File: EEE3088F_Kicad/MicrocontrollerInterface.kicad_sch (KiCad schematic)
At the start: 16 parts, among them J1 USB_B_Micro, U1 CAT24C256, U2 INTERFACE-CP2102-GMR(QFN28), U3 STM32F051C6Tx

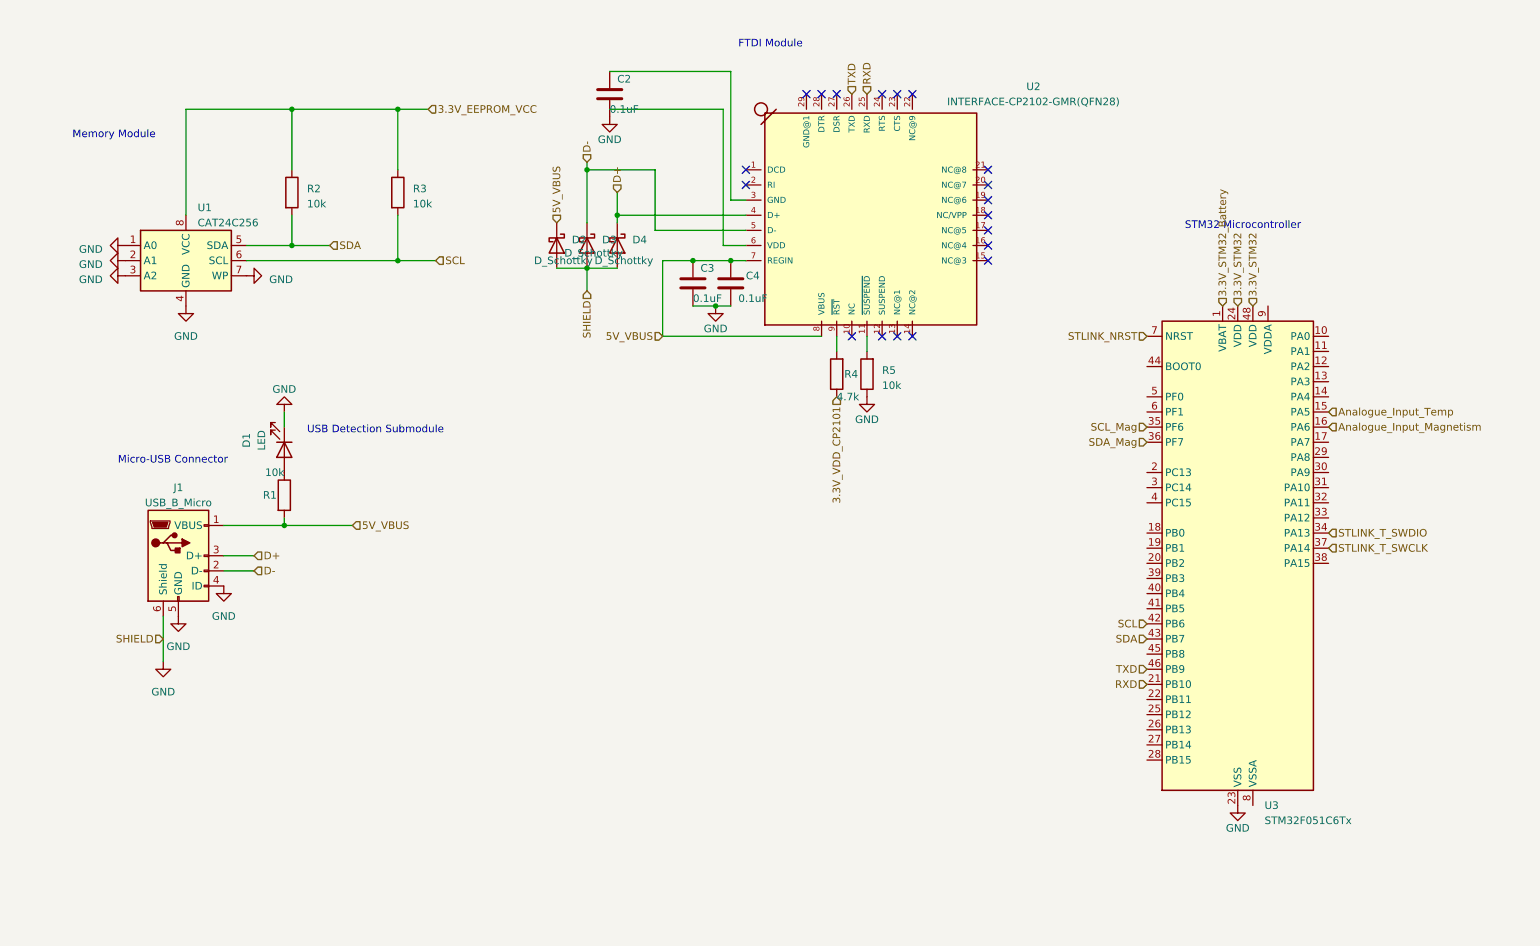
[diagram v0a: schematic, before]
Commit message: I have updated the microncontroller interface
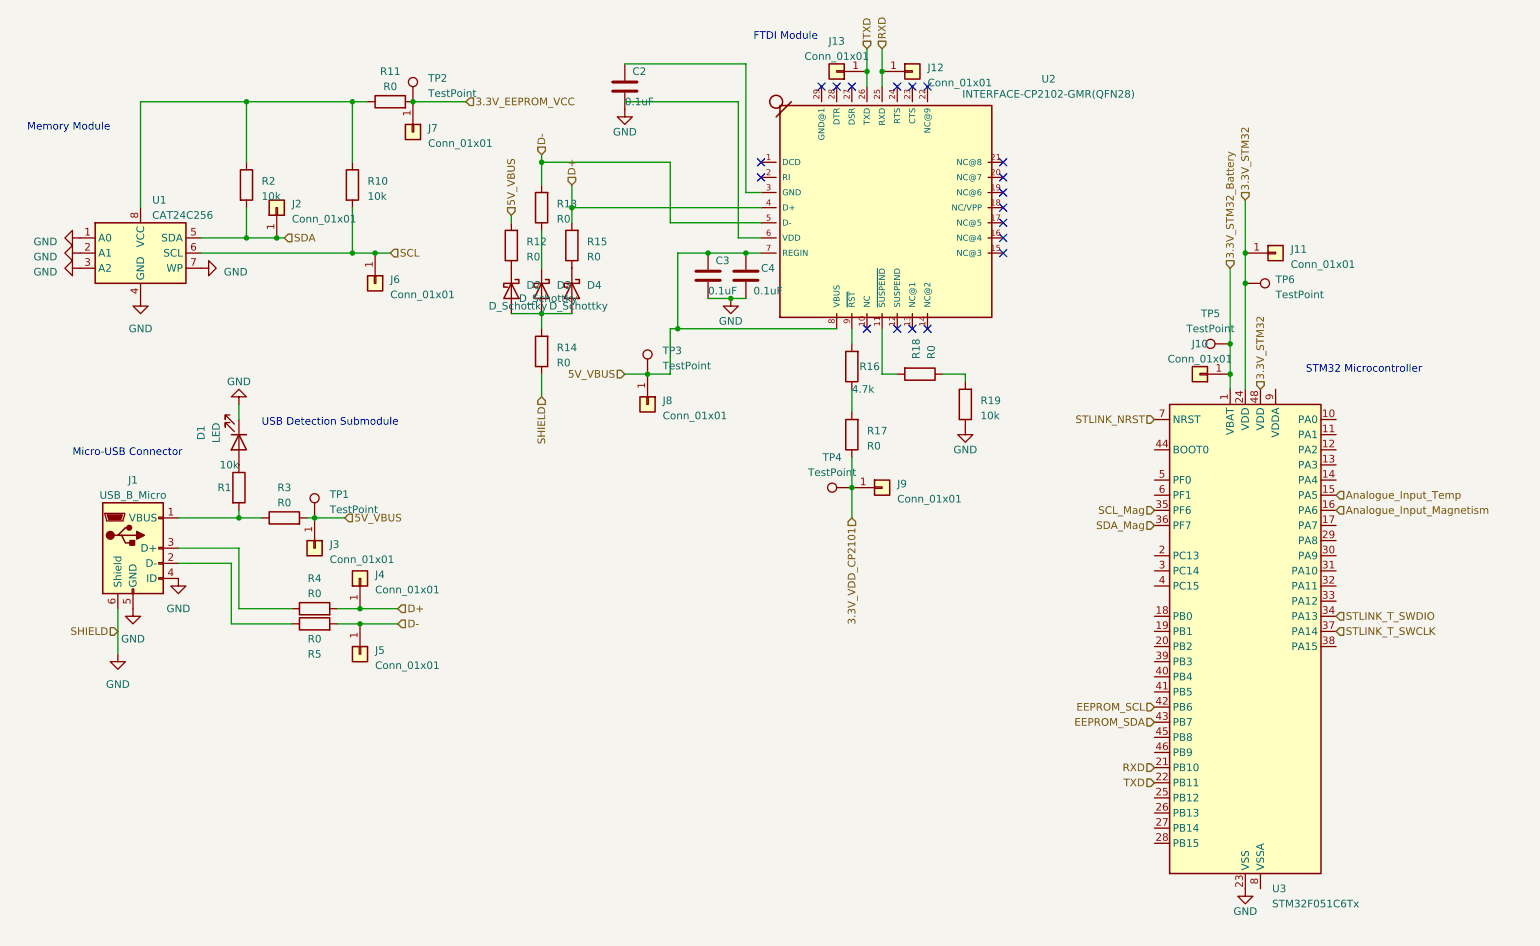
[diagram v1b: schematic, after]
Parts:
- added J10, J11, J12, J13, J2, J3, J4, J5, J6, J7, J8, J9: Conn_01x01, symbol Connector_Generic:Conn_01x01
- added R10, R19: 10k, symbol Device:R
- added R11, R12, R13, R14, R15, R17, R18: R0, symbol Device:R
- added R16: 4.7k, symbol Device:R
- added TP1, TP2, TP3, TP4, TP5, TP6: TestPoint, symbol Connector:TestPoint
- R3, R5: value 10k -> R0
- R4: value 4.7k -> R0
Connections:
- net 3.3V_EEPROM_VCC: now also J7.1 (Pin_1), R11.2, TP2.1; no longer R2.1, R3.1, U1.8 (VCC)
- net 3.3V_STM32: now also J11.1 (Pin_1), TP6.1
- net 3.3V_STM32_Battery: now also J10.1 (Pin_1), TP5.1
- net 3.3V_VDD_CP2101: now also J9.1 (Pin_1), R17.1, TP4.1; no longer R4.1
- net 5V_VBUS: now also R3.2, J3.1 (Pin_1), J8.1 (Pin_1), R12.2, TP1.1, TP3.1; no longer D2.1 (K), J1.1 (VBUS), R1.2
- net D+: now also R4.2, J4.1 (Pin_1), R15.2; no longer D4.1 (K), J1.3 (D+)
- net D-: now also R5.2, J5.1 (Pin_1), R13.2; no longer D3.1 (K), J1.2 (D-)
- net GND: now also R14.1, R19.1; no longer D2.2 (A), D3.2 (A), D4.2 (A), R5.1
- net RXD: now also J12.1 (Pin_1)
- net SCL: now also J6.1 (Pin_1), R10.2; no longer R3.2, U3.42 (PB6)
- net SDA: now also J2.1 (Pin_1); no longer U3.43 (PB7)
- net TXD: now also U3.22 (PB11), J13.1 (Pin_1); no longer U3.46 (PB9)
- net at U2.9 (~{RST}): now also R16.2; no longer R4.2
- net at U2.11 (~{SUSPEND}): now also R18.2; no longer R5.2
- new net: D3.1 (K), R13.1
- new net: R16.1, R17.2
- new net: D2.2 (A), D3.2 (A), D4.2 (A), R14.2
- new net: D4.1 (K), R15.1
- new net: R10.1, R11.1, R2.1, U1.8 (VCC)
- new net: J1.1 (VBUS), R1.2, R3.1
- new net: J1.2 (D-), R5.1
- new net: J1.3 (D+), R4.1
- new net: R18.1, R19.2
- new net: D2.1 (K), R12.1
- new net EEPROM_SCL: U3.42 (PB6)
- new net EEPROM_SDA: U3.43 (PB7)

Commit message: Microntroller Update
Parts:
- removed C2, C3, C4: 0.1uF, symbol Device:C
- removed D1: LED, symbol Device:LED
- removed D2, D3, D4: D_Schottky, symbol Device:D_Schottky
- removed J1: USB_B_Micro, symbol Connector:USB_B_Micro
- removed J10, J11, J12, J13, J2, J3, J4, J5, J6, J7, J8, J9: Conn_01x01, symbol Connector_Generic:Conn_01x01
- removed R1, R10, R2: 10k, symbol Device:R
- removed R11, R3, R4, R5: R0, symbol Device:R
- removed TP1, TP2, TP3, TP4, TP5, TP6: TestPoint, symbol Connector:TestPoint
- added C5, C6, C7: 0.1uF, symbol Device:C
- added D4: LED, symbol Device:LED
- added D5, D6, D7: D_Schottky, symbol Device:D_Schottky
- added J6: USB_B_Micro, MICROXNJ:SHOUHAN_MICROXNJ, symbol Connector:USB_B_Micro
- added R20, R21, R22, R24, R25, R27, R28: R0, symbol Device:R
- added R23: 4.7k, symbol Device:R
- added R26: 10k, symbol Device:R
- added TP10, TP11, TP12, TP13, TP14, TP15, TP16, TP7, TP8, TP9: TestPoint, symbol Connector:TestPoint
- R12, R13, R17: value R0 -> 10k; LCSC (none) -> C17902
- R14, R15, R18: LCSC (none) -> C17888
- R16: value 4.7k -> R0; LCSC (none) -> C17888
- R19: value 10k -> R0; LCSC (none) -> C17888
- U1: footprint (none) -> EEPROM:SOIC127P600X175-8N; LCSC (none) -> C6482
- U2: footprint QFN28G_0.5-5X5MM -> USB UART Chip:QFN28G_0.5-5X5MM; LCSC (none) -> C6568
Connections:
- net 3.3V_EEPROM_VCC: now also R18.2, TP10.1
- net 3.3V_STM32: now also R28.2; no longer U3.24 (VDD)
- net 3.3V_STM32_Battery: now also R27.2; no longer U3.1 (VBAT)
- net 3.3V_VDD_CP2101: now also R24.1, TP12.1; no longer R17.1
- net 5V_VBUS: now also R14.2, R19.2, C6.1, C7.1, TP11.1, TP7.1; no longer R12.2
- net D+: now also R22.2, TP8.1
- net D-: now also R16.2, R20.2, TP9.1; no longer R13.2
- net GND: now also C5.2, C6.2, C7.2, D4.1 (K), J6.4 (ID), J6.5 (GND), J6.6 (Shield), R21.1, R26.1; no longer R14.1, R19.1
- net RXD: now also TP14.1
- net SCL: now also R17.2
- net SDA: now also R13.2
- net TXD: now also TP13.1
- net at R13.1: now also R17.1, R18.1, U1.8 (VCC)
- net at R16.1: now also J6.2 (D-); no longer R17.2
- net at U2.9 (~{RST}): now also R23.2; no longer R16.2
- net at R15.1: now also J6.3 (D+)
- net at U2.3 (GND): now also C5.1
- net at R12.1: now also D4.2 (A)
- net at U2.11 (~{SUSPEND}): now also R25.2; no longer R18.2
- new net: R27.1, TP15.1, U3.1 (VBAT)
- new net: D5.2 (A), D6.2 (A), D7.2 (A), R21.2
- new net: D5.1 (K), R19.1
- new net: R25.1, R26.2
- new net: J6.1 (VBUS), R12.2, R14.1
- new net: D7.1 (K), R22.1
- new net: R28.1, TP16.1, U3.24 (VDD)
- new net: D6.1 (K), R20.1
- new net: R23.1, R24.2

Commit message: I have updated microcontoller and comments
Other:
- note added: "EEPROM chip that allows the environmental data to be stored to be retrived at a later date"
- note added: "STM32 micronctroller that facillites all the features of the device such as the retrieval of environmental as it communicates with the sensors and stores the data"
- note added: "The micro-USB Connector connects the board and STM32 microcontroller to the computer to facilate power and data transfer"
- note added: "This chip connects to the USB connector and allows the USB to interface with the STM32 microcontroller"
- title: (none) -> Microcontroller Interface
- moved on the sheet: D5, D6, R19, R20
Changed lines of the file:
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@@
 (kicad_sch (version 20230121) (generator eeschema)
   (paper "A4")
+  (title_block
+    (title "Microcontroller Interface")
+  )
   (junction (at 144.78 54.61) (diameter 0) (color 0 0 0 0)
   )
@@
   (junction (at 226.06 69.85) (diameter 0) (color 0 0 0 0)
   )
-  (junction (at 110.49 64.77) (diameter 0) (color 0 0 0 0)
+  (junction (at 106.68 64.77) (diameter 0) (color 0 0 0 0)
   )
   (junction (at 167.64 22.86) (diameter 0) (color 0 0 0 0)
@@
   (junction (at 81.28 114.3) (diameter 0) (color 0 0 0 0)
   )
-  (junction (at 110.49 39.37) (diameter 0) (color 0 0 0 0)
+  (junction (at 106.68 39.37) (diameter 0) (color 0 0 0 0)
   )
   (junction (at 228.6 59.69) (diameter 0) (color 0 0 0 0)
@@
   (no_connect (at 170.18 26.67))
   (no_connect (at 187.96 39.37))
-  (wire (pts (xy 110.49 39.37) (xy 110.49 43.18))
+  (wire (pts (xy 106.68 39.37) (xy 106.68 43.18))
     (stroke (width 0) (type default))
   )
@@
     (stroke (width 0) (type default))
   )
-  (wire (pts (xy 110.49 50.8) (xy 110.49 57.15))
+  (wire (pts (xy 106.68 50.8) (xy 106.68 57.15))
     (stroke (width 0) (type default))
   )
@@
     (stroke (width 0) (type default))
   )
-  (wire (pts (xy 110.49 38.1) (xy 110.49 39.37))
+  (wire (pts (xy 106.68 38.1) (xy 106.68 39.37))
     (stroke (width 0) (type default))
   )
@@
     (stroke (width 0) (type default))
   )
-  (wire (pts (xy 110.49 64.77) (xy 115.57 64.77))
+  (wire (pts (xy 106.68 64.77) (xy 115.57 64.77))
     (stroke (width 0) (type default))
   )
@@
     (stroke (width 0) (type default))
   )
+  (wire (pts (xy 106.68 66.04) (xy 110.49 66.04))
+    (stroke (width 0) (type default))
+  )
   (wire (pts (xy 167.64 19.05) (xy 167.64 22.86))
     (stroke (width 0) (type default))
@@
     (stroke (width 0) (type default))
   )
-  (wire (pts (xy 105.41 49.53) (xy 105.41 48.26))
+  (wire (pts (xy 95.25 49.53) (xy 95.25 48.26))
     (stroke (width 0) (type default))
   )
@@
     (stroke (width 0) (type default))
   )
-  (wire (pts (xy 110.49 64.77) (xy 110.49 67.31))
+  (wire (pts (xy 106.68 64.77) (xy 106.68 66.04))
     (stroke (width 0) (type default))
   )
@@
     (stroke (width 0) (type default))
   )
-  (wire (pts (xy 132.08 39.37) (xy 110.49 39.37))
+  (wire (pts (xy 132.08 39.37) (xy 106.68 39.37))
     (stroke (width 0) (type default))
   )
@@
     (stroke (width 0) (type default))
   )
-  (wire (pts (xy 105.41 64.77) (xy 110.49 64.77))
+  (wire (pts (xy 95.25 64.77) (xy 106.68 64.77))
     (stroke (width 0) (type default))
   )
@@
     (stroke (width 0) (type default))
   )
+  (wire (pts (xy 110.49 66.04) (xy 110.49 67.31))
+    (stroke (width 0) (type default))
+  )
   (wire (pts (xy 162.56 81.28) (xy 162.56 77.47))
     (stroke (width 0) (type default))
@@
   (wire (pts (xy 165.1 19.05) (xy 165.1 22.86))
     (stroke (width 0) (type default))
+  )
+  (text "STM32 micronctroller that facillites all the features\nof the device such as the retrieval of environmental\nas it communicates with the sensors and stores the data"
+    (at 153.67 148.59 0)
+    (effects (font (size 1.27 1.27)) (justify left bottom))
   )
   (text "STM32 Microcontroller" (at 238.76 74.93 0)
@@
     (effects (font (size 1.27 1.27)) (justify left bottom))
   )
+  (text "The micro-USB Connector connects the board and STM32 microcontroller\nto the computer to facilate power and data transfer"
+    (at 31.75 135.89 0)
+    (effects (font (size 1.27 1.27)) (justify left bottom))
+  )
   (text "USB Detection Submodule" (at 63.5 83.82 0)
     (effects (font (size 1.27 1.27)) (justify left bottom))
   )
+  (text "EEPROM chip that allows the environmental data\nto be stored to be retrived at a later date"
+    (at 26.67 72.39 0)
+    (effects (font (size 1.27 1.27)) (justify left bottom))
+  )
+  (text "This chip connects to the USB connector and allows the \nUSB to interface with the STM32 microcontroller"
+    (at 102.87 92.71 0)
+    (effects (font (size 1.27 1.27)) (justify left bottom))
+  )
   (text "FTDI Module" (at 146.05 19.05 0)
     (effects (font (size 1.27 1.27)) (justify left bottom))
@@
     (effects (font (size 1.27 1.27)) (justify left))
   )
-  (hierarchical_label "5V_VBUS" (shape input) (at 105.41 48.26 90) (fields_autoplaced)
+  (hierarchical_label "5V_VBUS" (shape input) (at 95.25 48.26 90) (fields_autoplaced)
     (effects (font (size 1.27 1.27)) (justify left))
   )
@@
     (effects (font (size 1.27 1.27)) (justify left))
   )
-  (hierarchical_label "D-" (shape input) (at 110.49 38.1 90) (fields_autoplaced)
+  (hierarchical_label "D-" (shape input) (at 106.68 38.1 90) (fields_autoplaced)
     (effects (font (size 1.27 1.27)) (justify left))
   )
@@
     )
   )
-  (symbol (lib_id "Device:D_Schottky") (at 105.41 60.96 270) (unit 1)
+  (symbol (lib_id "Device:D_Schottky") (at 95.25 60.96 270) (unit 1)
     (in_bom yes) (on_board yes) (dnp no)
-    (property "Reference" "D5" (at 107.95 60.0075 90)
-      (effects (font (size 1.27 1.27)) (justify left))
-    )
-    (property "Value" "D_Schottky" (at 101.6 63.5 90)
-      (effects (font (size 1.27 1.27)) (justify left))
-    )
-    (property "Footprint" "" (at 105.41 60.96 0)
-      (effects (font (size 1.27 1.27)) hide)
-    )
-    (property "Datasheet" "~" (at 105.41 60.96 0)
-      (effects (font (size 1.27 1.27)) hide)
-    )
-    (property "LCSC" "C7074" (at 105.41 60.96 0)
+    (property "Reference" "D5" (at 97.79 60.0075 90)
+      (effects (font (size 1.27 1.27)) (justify left))
+    )
+    (property "Value" "D_Schottky" (at 91.44 63.5 90)
+      (effects (font (size 1.27 1.27)) (justify left))
+    )
+    (property "Footprint" "" (at 95.25 60.96 0)
+      (effects (font (size 1.27 1.27)) hide)
+    )
+    (property "Datasheet" "~" (at 95.25 60.96 0)
+      (effects (font (size 1.27 1.27)) hide)
+    )
+    (property "LCSC" "C7074" (at 95.25 60.96 0)
       (effects (font (size 1.27 1.27)) hide)
     )
@@
     )
   )
-  (symbol (lib_id "Device:D_Schottky") (at 110.49 60.96 270) (unit 1)
+  (symbol (lib_id "Device:D_Schottky") (at 106.68 60.96 270) (unit 1)
     (in_bom yes) (on_board yes) (dnp no)
-    (property "Reference" "D6" (at 113.03 60.0075 90)
-      (effects (font (size 1.27 1.27)) (justify left))
-    )
-    (property "Value" "D_Schottky" (at 106.68 62.23 90)
-      (effects (font (size 1.27 1.27)) (justify left))
-    )
-    (property "Footprint" "" (at 110.49 60.96 0)
-      (effects (font (size 1.27 1.27)) hide)
-    )
-    (property "Datasheet" "~" (at 110.49 60.96 0)
-      (effects (font (size 1.27 1.27)) hide)
-    )
-    (property "LCSC" "C7074" (at 110.49 60.96 0)
+    (property "Reference" "D6" (at 109.22 60.0075 90)
+      (effects (font (size 1.27 1.27)) (justify left))
+    )
+    (property "Value" "D_Schottky" (at 102.87 55.88 90)
+      (effects (font (size 1.27 1.27)) (justify left))
+    )
+    (property "Footprint" "" (at 106.68 60.96 0)
+      (effects (font (size 1.27 1.27)) hide)
+    )
+    (property "Datasheet" "~" (at 106.68 60.96 0)
+      (effects (font (size 1.27 1.27)) hide)
+    )
+    (property "LCSC" "C7074" (at 106.68 60.96 0)
       (effects (font (size 1.27 1.27)) hide)
     )
@@
     )
   )
-  (symbol (lib_id "Device:R") (at 105.41 53.34 180) (unit 1)
-    (in_bom yes) (on_board yes) (dnp no) (fields_autoplaced)
-    (property "Reference" "R19" (at 107.95 52.705 0)
-      (effects (font (size 1.27 1.27)) (justify right))
-    )
-    (property "Value" "R0" (at 107.95 55.245 0)
-      (effects (font (size 1.27 1.27)) (justify right))
-    )
-    (property "Footprint" "" (at 107.188 53.34 90)
-      (effects (font (size 1.27 1.27)) hide)
-    )
-    (property "Datasheet" "~" (at 105.41 53.34 0)
-      (effects (font (size 1.27 1.27)) hide)
-    )
-    (property "LCSC" "C17888" (at 105.41 53.34 0)
+  (symbol (lib_id "Device:R") (at 95.25 53.34 180) (unit 1)
+    (in_bom yes) (on_board yes) (dnp no) (fields_autoplaced)
+    (property "Reference" "R19" (at 97.79 52.705 0)
+      (effects (font (size 1.27 1.27)) (justify right))
+    )
+    (property "Value" "R0" (at 97.79 55.245 0)
+      (effects (font (size 1.27 1.27)) (justify right))
+    )
+    (property "Footprint" "" (at 97.028 53.34 90)
+      (effects (font (size 1.27 1.27)) hide)
+    )
+    (property "Datasheet" "~" (at 95.25 53.34 0)
+      (effects (font (size 1.27 1.27)) hide)
+    )
+    (property "LCSC" "C17888" (at 95.25 53.34 0)
       (effects (font (size 1.27 1.27)) hide)
     )
@@
     )
   )
-  (symbol (lib_id "Device:R") (at 110.49 46.99 180) (unit 1)
-    (in_bom yes) (on_board yes) (dnp no) (fields_autoplaced)
-    (property "Reference" "R20" (at 113.03 46.355 0)
-      (effects (font (size 1.27 1.27)) (justify right))
-    )
-    (property "Value" "R0" (at 113.03 48.895 0)
-      (effects (font (size 1.27 1.27)) (justify right))
-    )
-    (property "Footprint" "" (at 112.268 46.99 90)
-      (effects (font (size 1.27 1.27)) hide)
-    )
-    (property "Datasheet" "~" (at 110.49 46.99 0)
-      (effects (font (size 1.27 1.27)) hide)
-    )
-    (property "LCSC" "C17888" (at 110.49 46.99 0)
-      (effects (font (size 1.27 1.27)) hide)
-    )
+  (symbol (lib_id "Device:R") (at 106.68 46.99 180) (unit 1)
+    (in_bom yes) (on_board yes) (dnp no) (fields_autoplaced)
+    (property "Reference" "R20" (at 109.22 46.355 0)
+      (effects (font (size 1.27 1.27)) (justify right))
+    )
+    (property "Value" "R0" (at 109.22 48.895 0)
+      (effects (font (size 1.27 1.27)) (justify right))
+    )
+    (property "Footprint" "" (at 108.458 46.99 90)
+      (effects (font (size 1.27 1.27)) hide)
+    )
+    (property "Datasheet" "~" (at 106.68 46.99 0)
+      (effects (font (size 1.27 1.27)) hide)
+    )
+    (property "LCSC" "C17888" (at 106.68 46.99 0)
+      (effects (font (size 1.27 1.27)) hide)
+    )

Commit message: added the external connections between subsystems
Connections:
- net SCL is gone; now on net EEPROM_SCL: R17.2, U1.6 (SCL)
- net SDA is gone; now on net EEPROM_SDA: R13.2, U1.5 (SDA)
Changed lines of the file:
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@@
     (stroke (width 0) (type default))
   )
-  (wire (pts (xy 78.74 54.61) (xy 85.09 54.61))
+  (wire (pts (xy 78.74 54.61) (xy 80.01 54.61))
     (stroke (width 0) (type default))
   )
@@
     (stroke (width 0) (type default))
   )
-  (wire (pts (xy 60.96 52.07) (xy 67.31 52.07))
+  (wire (pts (xy 60.96 52.07) (xy 64.77 52.07))
     (stroke (width 0) (type default))
   )
@@
     (effects (font (size 1.27 1.27)) (justify left))
   )
-  (hierarchical_label "SCL" (shape input) (at 85.09 54.61 0) (fields_autoplaced)
+  (hierarchical_label "EEPROM_SCL" (shape input) (at 80.01 54.61 0) (fields_autoplaced)
     (effects (font (size 1.27 1.27)) (justify left))
   )
@@
     (effects (font (size 1.27 1.27)) (justify right))
   )
-  (hierarchical_label "SDA" (shape input) (at 67.31 52.07 0) (fields_autoplaced)
+  (hierarchical_label "EEPROM_SDA" (shape input) (at 64.77 52.07 0) (fields_autoplaced)
     (effects (font (size 1.27 1.27)) (justify left))
   )
@@
     (effects (font (size 1.27 1.27)) (justify left))
   )
-  (hierarchical_label "5V_VBUS" (shape input) (at 77.47 99.06 0) (fields_autoplaced)
+  (hierarchical_label "5V_VBUS" (shape output) (at 77.47 99.06 0) (fields_autoplaced)
     (effects (font (size 1.27 1.27)) (justify left))
   )
